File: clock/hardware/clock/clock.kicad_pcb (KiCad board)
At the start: 2 copper layers, 45.7 x 58.4 mm, 27 parts, among them J1 USB_B_Micro, J2 7SEG_DEBUG, J3 Conn_ARM_JTAG_SWD_10, U1 LM1117-3.3, U2 AS1115, U3 LTC-4727JS, U4 STM32L151C8TxA, Y1 32.768kHz

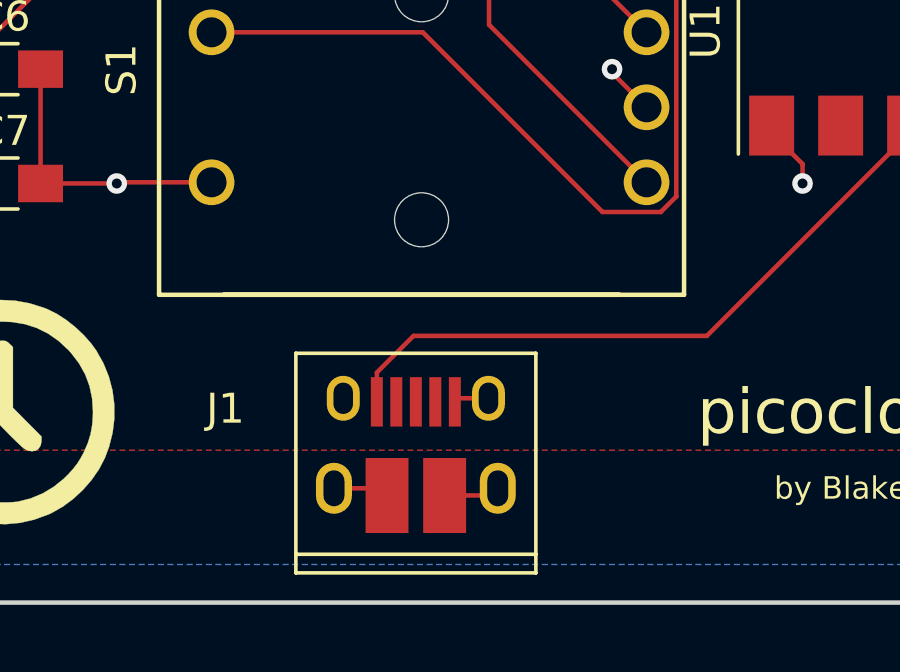
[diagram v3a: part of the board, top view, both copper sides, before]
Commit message: Change to non-slotted USB connector
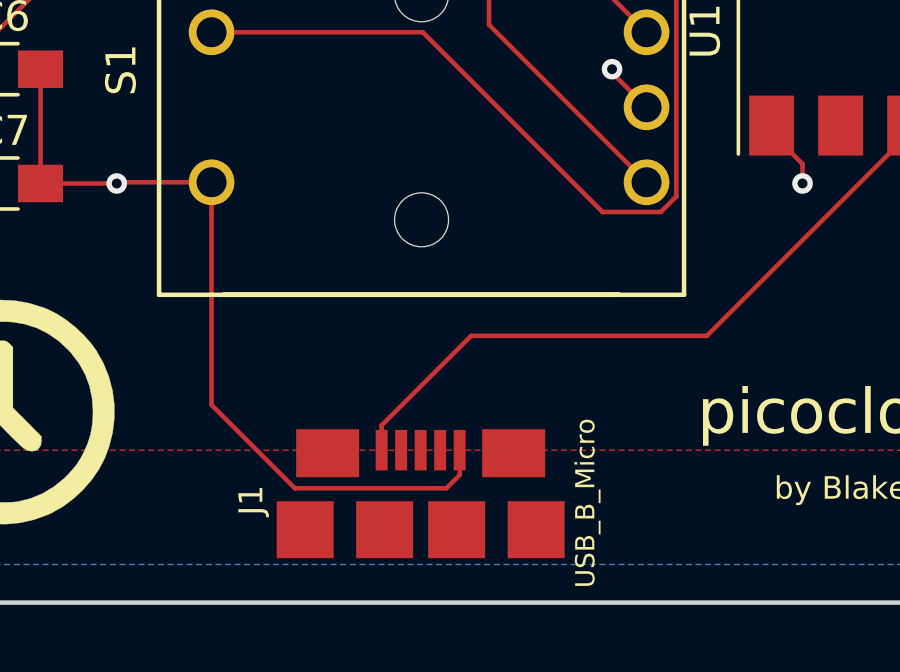
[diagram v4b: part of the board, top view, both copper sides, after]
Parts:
- J1: footprint Connectors:USB_Micro-B_10103594-0001LF -> custom_connectors:10118192-0001LF
- moved J1 4.21 mm to (83.8, 76.5)
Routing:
- net GND: track 80.3 -> 93.1 mm
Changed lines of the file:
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@@
     (thickness 1.6)
     (drawings 8)
-    (tracks 279)
+    (tracks 278)
     (zones 0)
     (modules 27)
@@
     )
   )
-  (module Connectors:USB_Micro-B_10103594-0001LF (layer F.Cu)
-    (at 83.63 72.28)
-    (descr "Micro USB Type B 10103594-0001LF")
-    (tags "USB USB_B USB_micro USB_OTG")
-    (attr smd)
-    (fp_text reference J1 (at -6.35 -1.27) (layer F.SilkS)
-      (effects (font (size 1 1) (thickness 0.15)))
-    )
-    (fp_text value USB_B_Micro (at 0 -4.97) (layer F.Fab)
-      (effects (font (size 1 1) (thickness 0.15)))
-    )
-    (fp_line (start -4 4.2) (end -4 -3.12) (layer F.SilkS) (width 0.12))
-    (fp_line (start 4 3.58) (end -4 3.58) (layer F.SilkS) (width 0.12))
-    (fp_line (start 4 -3.12) (end 4 4.2) (layer F.SilkS) (width 0.12))
-    (fp_line (start -4 -3.12) (end 4 -3.12) (layer F.SilkS) (width 0.12))
-    (fp_line (start -4 4.2) (end 4 4.2) (layer F.SilkS) (width 0.12))
-    (fp_line (start -4.25 4.45) (end -4.25 -3.4) (layer F.CrtYd) (width 0.05))
-    (fp_line (start 4.25 4.45) (end -4.25 4.45) (layer F.CrtYd) (width 0.05))
-    (fp_line (start 4.25 -3.4) (end 4.25 4.45) (layer F.CrtYd) (width 0.05))
-    (fp_line (start -4.25 -3.4) (end 4.25 -3.4) (layer F.CrtYd) (width 0.05))
-    (pad 6 smd rect (at 0.96 1.62 90) (size 2.5 1.43) (layers F.Cu F.Paste F.Mask)
-      (net 2 GND))
-    (pad 6 smd rect (at -0.96 1.62 90) (size 2.5 1.43) (layers F.Cu F.Paste F.Mask)
-      (net 2 GND))
-    (pad 6 thru_hole oval (at 2.73 1.38 90) (size 1.7 1.2) (drill oval 1.2 0.7) (layers *.Cu *.Mask)
-      (net 2 GND))
-    (pad 6 thru_hole oval (at -2.73 1.38 90) (size 1.7 1.2) (drill oval 1.2 0.7) (layers *.Cu *.Mask)
-      (net 2 GND))
-    (pad 6 thru_hole oval (at 2.42 -1.62 90) (size 1.5 1.1) (drill oval 1.05 0.65) (layers *.Cu *.Mask)
-      (net 2 GND))
-    (pad 6 thru_hole oval (at -2.42 -1.62 90) (size 1.5 1.1) (drill oval 1.05 0.65) (layers *.Cu *.Mask)
-      (net 2 GND))
-    (pad 5 smd rect (at 1.3 -1.5 90) (size 1.65 0.4) (layers F.Cu F.Paste F.Mask)
-      (net 2 GND))
-    (pad 4 smd rect (at 0.65 -1.5 90) (size 1.65 0.4) (layers F.Cu F.Paste F.Mask)
-      (net 10 "Net-(J1-Pad4)"))
-    (pad 3 smd rect (at 0 -1.5 90) (size 1.65 0.4) (layers F.Cu F.Paste F.Mask)
-      (net 11 "Net-(J1-Pad3)"))
-    (pad 2 smd rect (at -0.65 -1.5 90) (size 1.65 0.4) (layers F.Cu F.Paste F.Mask)
-      (net 12 "Net-(J1-Pad2)"))
-    (pad 1 smd rect (at -1.3 -1.5 90) (size 1.65 0.4) (layers F.Cu F.Paste F.Mask)
-      (net 13 "Net-(J1-Pad1)"))
-  )
   (module Pin_Headers:Pin_Header_Straight_1x04_Pitch2.54mm (layer F.Cu)
     (at 80.01 21.59 90)
@@
       (rotate (xyz 0 0 0))
     )
+  )
+  (module custom_connectors:10118192-0001LF (layer F.Cu)
+    (at 83.79 76.49)
+    (descr "USB MICRO B<p>FCI")
+    (solder_mask_margin 0.1)
+    (attr smd)
+    (fp_text reference J1 (at -5.648 -2.432 90) (layer F.SilkS)
+      (effects (font (size 0.8 0.8) (thickness 0.05)))
+    )
+    (fp_text value USB_B_Micro (at 5.4936 -2.332 90) (layer F.SilkS)
+      (effects (font (size 0.64 0.64) (thickness 0.05)))
+    )
+    (fp_arc (start 4.0456 0.700072) (end 3.9 0.7) (angle -37.9) (layer Dwgs.User) (width 0.0508))
+    (fp_line (start 4.25 1.2) (end 3.9307 0.7895) (layer Dwgs.User) (width 0.0508))
+    (fp_line (start 3.6 0.7093) (end 3.6 0.7) (layer Dwgs.User) (width 0.0508))
+    (fp_arc (start 3.854 0.709376) (end 3.6 0.7093) (angle -39.3) (layer Dwgs.User) (width 0.0508))
+    (fp_line (start 4.05 1.35) (end 3.6574 0.8702) (layer Dwgs.User) (width 0.0508))
+    (fp_line (start 4.25 1.2) (end 4.05 1.35) (layer Dwgs.User) (width 0.0508))
+    (fp_arc (start -4.0457 0.700038) (end -3.9 0.7) (angle 37.8) (layer Dwgs.User) (width 0.0508))
+    (fp_line (start -4.25 1.2) (end -3.9307 0.7895) (layer Dwgs.User) (width 0.0508))
+    (fp_line (start -3.6 0.7093) (end -3.6 0.7) (layer Dwgs.User) (width 0.0508))
+    (fp_arc (start -3.854 0.709376) (end -3.6 0.7093) (angle 39.3) (layer Dwgs.User) (width 0.0508))
+    (fp_line (start -4.05 1.35) (end -3.6574 0.8702) (layer Dwgs.User) (width 0.0508))
+    (fp_line (start -4.25 1.2) (end -4.05 1.35) (layer Dwgs.User) (width 0.0508))
+    (fp_line (start 3.85 0) (end -3.85 0) (layer Dwgs.User) (width 0))
+    (fp_arc (start 2.9 0.95) (end 2.9 1.2) (angle -53.1) (layer Dwgs.User) (width 0.0508))
+    (fp_arc (start -2.925 1) (end -3.1 1.1) (angle -67.3) (layer Dwgs.User) (width 0.0508))
+    (fp_line (start 2.9 1.2) (end -2.9 1.2) (layer Dwgs.User) (width 0.0508))
+    (fp_line (start -3.9 0.7) (end -3.9 -4.3) (layer Dwgs.User) (width 0.0508))
+    (fp_line (start -3.6 0.7) (end -3.9 0.7) (layer Dwgs.User) (width 0.0508))
+    (fp_line (start -3.1 0.7) (end -3.6 0.7) (layer Dwgs.User) (width 0.0508))
+    (fp_line (start -3.1 1.1) (end -3.1 0.7) (layer Dwgs.User) (width 0.0508))
+    (fp_arc (start -2.9 1.1) (end -3.1 1.1) (angle -90) (layer Dwgs.User) (width 0.0508))
+    (fp_line (start 2.9 1.3) (end -2.9 1.3) (layer Dwgs.User) (width 0.0508))
+    (fp_arc (start 2.9 1.1) (end 2.9 1.3) (angle -90) (layer Dwgs.User) (width 0.0508))
+    (fp_line (start 3.1 0.7) (end 3.1 1.1) (layer Dwgs.User) (width 0.0508))
+    (fp_line (start 3.9 0.7) (end 3.1 0.7) (layer Dwgs.User) (width 0.0508))
+    (fp_line (start 3.9 -4.3) (end 3.9 0.7) (layer Dwgs.User) (width 0.0508))
+    (fp_line (start -3.9 -4.3) (end 3.9 -4.3) (layer Dwgs.User) (width 0.0508))
+    (pad S2 smd rect (at 3.85 -1.45) (size 1.9 1.9) (layers F.Cu F.Paste F.Mask)
+      (solder_mask_margin 0.2))
+    (pad S4 smd rect (at 3.1 -4) (size 2.1 1.6) (layers F.Cu F.Paste F.Mask)
+      (solder_mask_margin 0.2))
+    (pad S3 smd rect (at -3.1 -4) (size 2.1 1.6) (layers F.Cu F.Paste F.Mask)
+      (solder_mask_margin 0.2))
+    (pad S1 smd rect (at -3.85 -1.45) (size 1.9 1.9) (layers F.Cu F.Paste F.Mask)
+      (solder_mask_margin 0.2))
+    (pad M2 smd rect (at 1.2 -1.45) (size 1.9 1.9) (layers F.Cu F.Paste F.Mask)
+      (solder_mask_margin 0.2))
+    (pad M1 smd rect (at -1.2 -1.45) (size 1.9 1.9) (layers F.Cu F.Paste F.Mask)
+      (solder_mask_margin 0.2))
+    (pad 5 smd rect (at 1.3 -4.1 90) (size 1.35 0.4) (layers F.Cu F.Paste F.Mask)
+      (net 2 GND) (solder_mask_margin 0.2))
+    (pad 4 smd rect (at 0.65 -4.1 90) (size 1.35 0.4) (layers F.Cu F.Paste F.Mask)
+      (net 10 "Net-(J1-Pad4)") (solder_mask_margin 0.2))
+    (pad 3 smd rect (at 0 -4.1 90) (size 1.35 0.4) (layers F.Cu F.Paste F.Mask)
+      (net 11 "Net-(J1-Pad3)") (solder_mask_margin 0.2))
+    (pad 2 smd rect (at -0.65 -4.1 90) (size 1.35 0.4) (layers F.Cu F.Paste F.Mask)
+      (net 12 "Net-(J1-Pad2)") (solder_mask_margin 0.2))
+    (pad 1 smd rect (at -1.3 -4.1 90) (size 1.35 0.4) (layers F.Cu F.Paste F.Mask)
+      (net 13 "Net-(J1-Pad1)") (solder_mask_margin 0.2))
   )
   (gr_text "by Blake" (at 97.79 73.66) (layer F.SilkS)
@@
   (segment (start 84.391501 53.911501) (end 90.335899 53.911501) (width 0.1524) (layer B.Cu) (net 2))
   (segment (start 83.82 53.34) (end 84.391501 53.911501) (width 0.1524) (layer B.Cu) (net 2))
-  (segment (start 81.33 70.78) (end 81.21 70.66) (width 0.1524) (layer B.Cu) (net 2))
-  (segment (start 82.43 73.66) (end 82.67 73.9) (width 0.1524) (layer F.Cu) (net 2))
-  (segment (start 80.9 73.66) (end 82.43 73.66) (width 0.1524) (layer F.Cu) (net 2))
-  (segment (start 86.12 73.9) (end 86.36 73.66) (width 0.1524) (layer F.Cu) (net 2))
-  (segment (start 84.59 73.9) (end 86.12 73.9) (width 0.1524) (layer F.Cu) (net 2))
-  (segment (start 85.05 70.66) (end 84.93 70.78) (width 0.1524) (layer F.Cu) (net 2))
-  (segment (start 86.05 70.66) (end 85.05 70.66) (width 0.1524) (layer F.Cu) (net 2))
   (via (at 73.66 63.5) (size 0.6858) (drill 0.3302) (layers F.Cu B.Cu) (net 2))
   (segment (start 71.12 63.5) (end 73.66 63.5) (width 0.1524) (layer F.Cu) (net 2))
   (segment (start 73.7 63.46) (end 73.66 63.5) (width 0.1524) (layer F.Cu) (net 2))
   (segment (start 76.82 63.46) (end 73.7 63.46) (width 0.1524) (layer F.Cu) (net 2))
+  (segment (start 85.09 73.2174) (end 84.6474 73.66) (width 0.1524) (layer F.Cu) (net 2))
+  (segment (start 85.09 72.39) (end 85.09 73.2174) (width 0.1524) (layer F.Cu) (net 2))
+  (segment (start 76.82 64.53763) (end 76.82 63.46) (width 0.1524) (layer F.Cu) (net 2))
+  (segment (start 79.598518 73.66) (end 76.82 70.881482) (width 0.1524) (layer F.Cu) (net 2))
+  (segment (start 76.82 70.881482) (end 76.82 64.53763) (width 0.1524) (layer F.Cu) (net 2))
+  (segment (start 84.6474 73.66) (end 79.598518 73.66) (width 0.1524) (layer F.Cu) (net 2))
   (segment (start 69.398601 54.701399) (end 68.62 55.48) (width 0.1524) (layer F.Cu) (net 3))
   (segment (start 79.395083 54.701399) (end 69.398601 54.701399) (width 0.1524) (layer F.Cu) (net 3))
@@
   (segment (start 88.17 48.24) (end 93.4524 48.24) (width 0.1524) (layer F.Cu) (net 8))
   (segment (start 97.87 45.72) (end 101.44 45.72) (width 0.1524) (layer F.Cu) (net 9))
+  (segment (start 100.09 61.82) (end 93.33 68.58) (width 0.1524) (layer F.Cu) (net 13))
   (segment (start 100.09 61.57) (end 100.09 61.82) (width 0.1524) (layer F.Cu) (net 13))
-  (segment (start 82.33 69.8026) (end 82.33 70.78) (width 0.1524) (layer F.Cu) (net 13))
-  (segment (start 100.09 61.82) (end 93.33 68.58) (width 0.1524) (layer F.Cu) (net 13))
-  (segment (start 93.33 68.58) (end 83.5526 68.58) (width 0.1524) (layer F.Cu) (net 13))
-  (segment (start 83.5526 68.58) (end 82.33 69.8026) (width 0.1524) (layer F.Cu) (net 13))
+  (segment (start 82.49 71.5626) (end 82.49 72.39) (width 0.1524) (layer F.Cu) (net 13))
+  (segment (start 85.4726 68.58) (end 82.49 71.5626) (width 0.1524) (layer F.Cu) (net 13))
+  (segment (start 93.33 68.58) (end 85.4726 68.58) (width 0.1524) (layer F.Cu) (net 13))
   (via (at 93.98 35.56) (size 0.6858) (drill 0.3302) (layers F.Cu B.Cu) (net 14))
   (segment (start 95.25 36.83) (end 93.98 35.56) (width 0.1524) (layer B.Cu) (net 14))

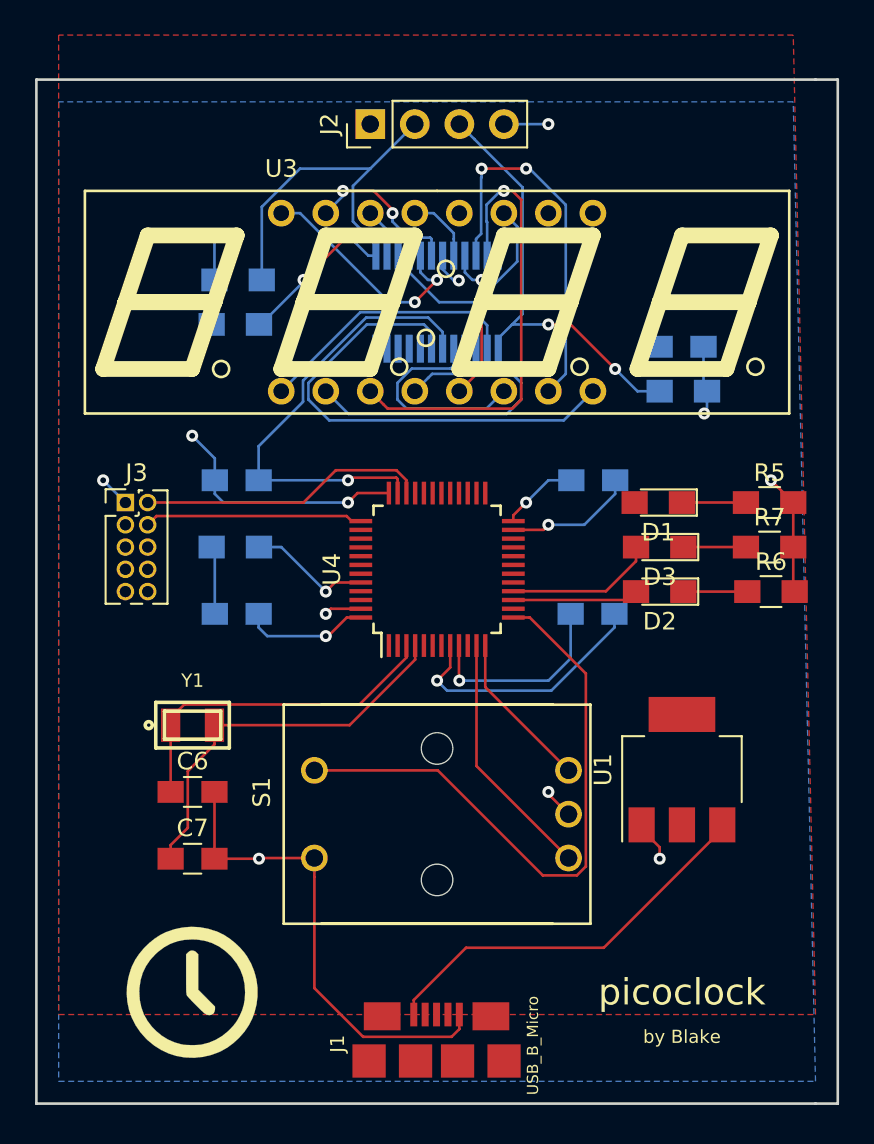
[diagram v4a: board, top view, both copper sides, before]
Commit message: Rev B. of clock. Power rails. SMD JTAG connector.
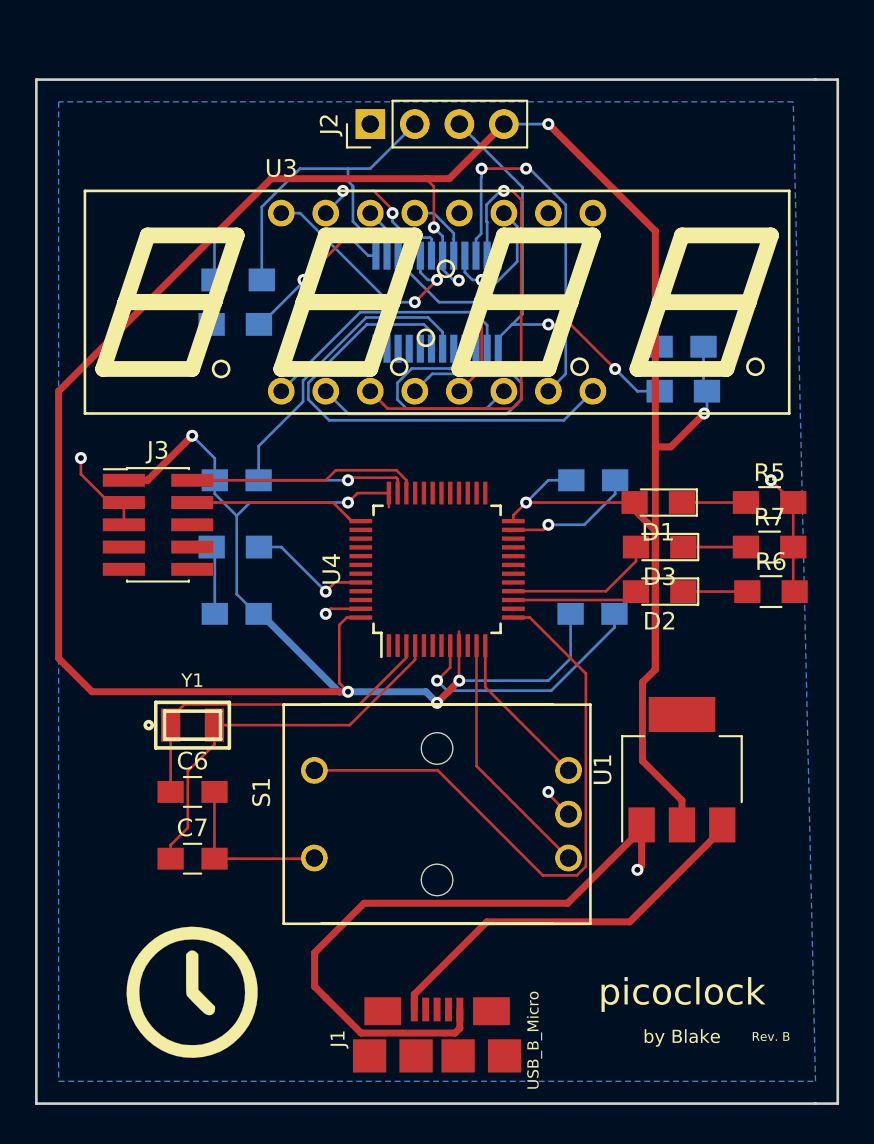
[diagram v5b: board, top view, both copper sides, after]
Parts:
- J3: footprint Pin_Headers:Pin_Header_Straight_2x05_Pitch1.27mm -> Pin_Headers:Pin_Header_Straight_2x05_Pitch1.27mm_SMD
- moved J3 2.25 mm to (67.9, 44.5)
- moved J1 0.29 mm to (83.8, 76.2)
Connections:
- J3 pad 9: GND -> Net-(J3-Pad9)
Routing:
- net +3V3: track 52.8 -> 208.8 mm, vias 10 -> 11
- net GND: track 93.1 -> 116.1 mm
- net /JTAG_TMS: track 16.5 -> 13.4 mm
- net /JTAG_TCK: track 12.5 -> 10.5 mm
- removed copper zone on F.Cu, net +3V3
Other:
- net class 3v added: clearance 0.1524, trace_width 0.1524, via_dia 0.6858, via_drill 0.3302
- net class 5v added: clearance 0.1524, trace_width 0.4, via_dia 0.9, via_drill 0.3302
- net class GndRail added: clearance 0.1524, trace_width 0.4, via_dia 0.6858, via_drill 0.3302
- board text added: "Rev. B"

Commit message: Route initial USB ground directly to regulator.
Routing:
- net GND: track 116.1 -> 96.1 mm, vias 8 -> 9
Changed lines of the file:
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@@
     (thickness 1.6)
     (drawings 9)
-    (tracks 332)
+    (tracks 329)
     (zones 0)
     (modules 27)
@@
   (segment (start 76.78 63.5) (end 76.82 63.46) (width 0.1524) (layer F.Cu) (net 2))
   (segment (start 71.12 63.5) (end 76.78 63.5) (width 0.1524) (layer F.Cu) (net 2))
-  (segment (start 79.483277 73.447599) (end 77.47 71.434322) (width 0.4) (layer F.Cu) (net 2))
-  (segment (start 84.847401 73.447599) (end 79.483277 73.447599) (width 0.4) (layer F.Cu) (net 2))
-  (segment (start 85.12 73.175) (end 84.847401 73.447599) (width 0.4) (layer F.Cu) (net 2))
-  (segment (start 85.12 72.1) (end 85.12 73.175) (width 0.4) (layer F.Cu) (net 2))
-  (segment (start 77.47 71.434322) (end 76.835 70.799322) (width 0.4) (layer F.Cu) (net 2))
-  (segment (start 76.835 68.860678) (end 79.655678 66.04) (width 0.4) (layer F.Cu) (net 2))
-  (segment (start 76.835 70.799322) (end 76.835 68.860678) (width 0.4) (layer F.Cu) (net 2))
-  (segment (start 91.27 66.04) (end 95.49 61.82) (width 0.4) (layer F.Cu) (net 2))
   (segment (start 95.49 61.82) (end 95.49 61.57) (width 0.4) (layer F.Cu) (net 2))
-  (segment (start 79.655678 66.04) (end 91.27 66.04) (width 0.4) (layer F.Cu) (net 2))
   (segment (start 95.49 61.57) (end 95.49 62.47) (width 0.4) (layer F.Cu) (net 2))
   (via (at 95.25 64.135) (size 0.6858) (drill 0.3302) (layers F.Cu B.Cu) (net 2))
   (segment (start 95.49 63.895) (end 95.25 64.135) (width 0.4) (layer F.Cu) (net 2))
   (segment (start 95.49 61.57) (end 95.49 63.895) (width 0.4) (layer F.Cu) (net 2))
+  (via (at 92.075 67.945) (size 0.6858) (drill 0.3302) (layers F.Cu B.Cu) (net 2))
+  (segment (start 88.8 67.945) (end 92.075 67.945) (width 0.4) (layer F.Cu) (net 2))
+  (segment (start 85.12 71.625) (end 88.8 67.945) (width 0.4) (layer F.Cu) (net 2))
+  (segment (start 85.12 72.1) (end 85.12 71.625) (width 0.4) (layer F.Cu) (net 2))
+  (segment (start 92.075 67.31) (end 95.25 64.135) (width 0.4) (layer B.Cu) (net 2))
+  (segment (start 92.075 67.945) (end 92.075 67.31) (width 0.4) (layer B.Cu) (net 2))
   (segment (start 69.398601 54.701399) (end 68.62 55.48) (width 0.1524) (layer F.Cu) (net 3))
   (segment (start 79.395083 54.701399) (end 69.398601 54.701399) (width 0.1524) (layer F.Cu) (net 3))
